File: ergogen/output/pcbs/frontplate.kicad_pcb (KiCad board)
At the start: 2 copper layers, 134 x 92.7 mm, 0 parts

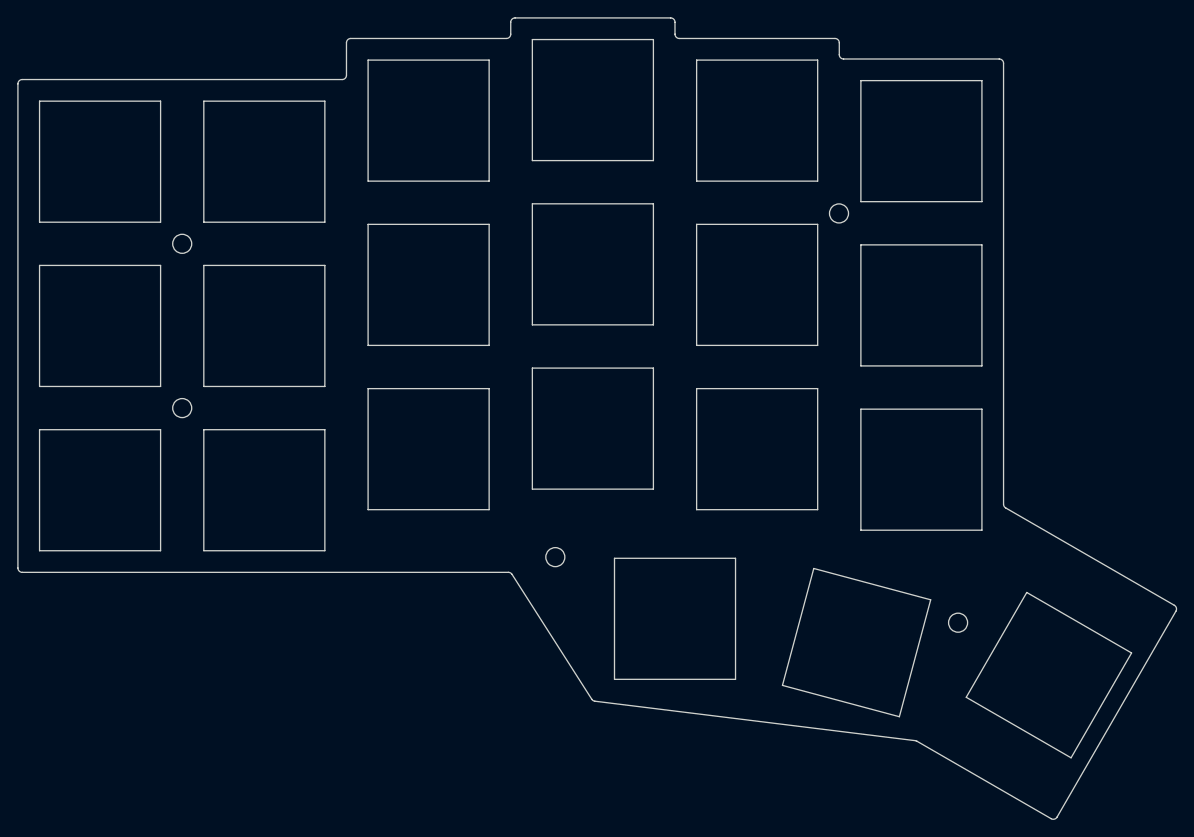
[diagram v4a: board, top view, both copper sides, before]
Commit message: Overhaul outlines making use of intersect
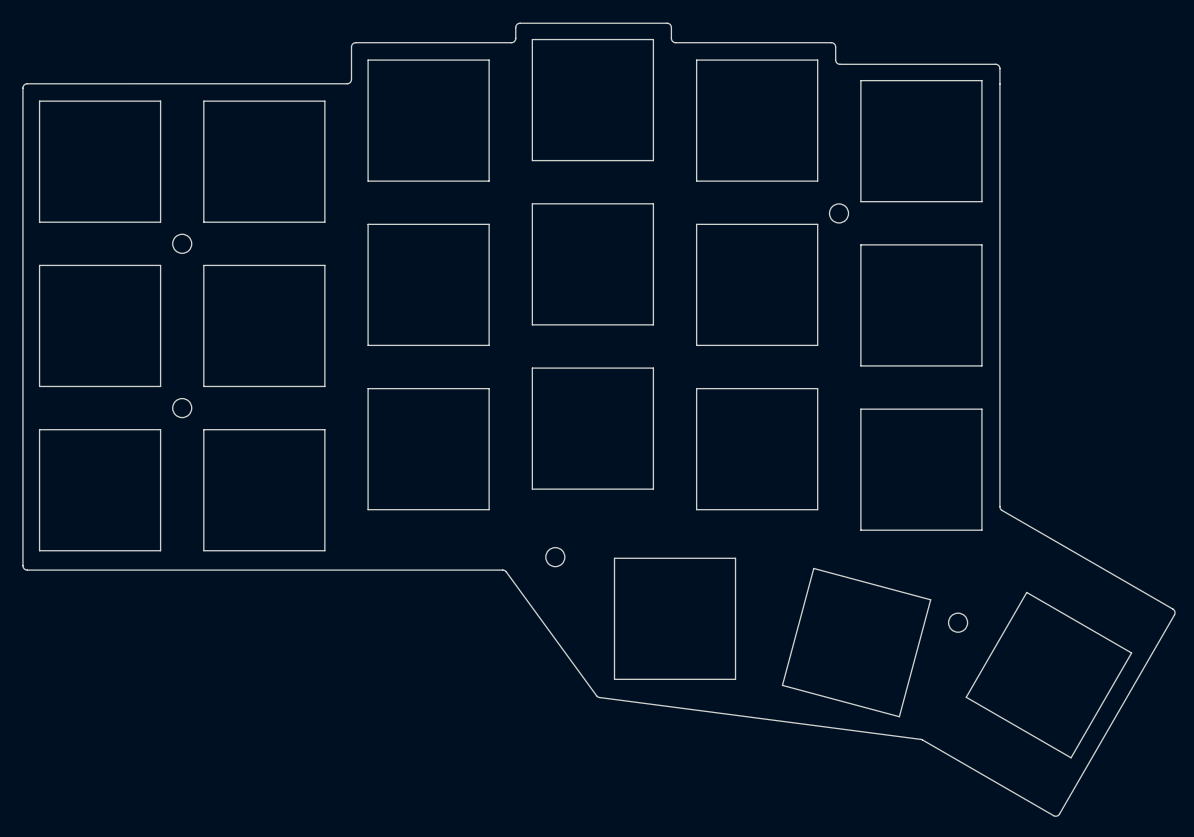
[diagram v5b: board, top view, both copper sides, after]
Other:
- board size 134 x 92.7 mm -> 133.3 x 91.7 mm
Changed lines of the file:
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@@
     (add_net "")
   )
-            (gr_line (start 91 109.5) (end 147.226056907563 109.5) (angle 90) (layer Edge.Cuts) (width 0.15))
-(gr_line (start 90.5 109) (end 90.5 53) (angle 90) (layer Edge.Cuts) (width 0.15))
-(gr_line (start 91 52.5) (end 128 52.5) (angle 90) (layer Edge.Cuts) (width 0.15))
-(gr_line (start 147 47.75) (end 129 47.75) (angle 90) (layer Edge.Cuts) (width 0.15))
-(gr_line (start 128.5 48.25) (end 128.5 52) (angle 90) (layer Edge.Cuts) (width 0.15))
-(gr_line (start 166.5 47.25) (end 166.5 45.875) (angle 90) (layer Edge.Cuts) (width 0.15))
-(gr_line (start 166 45.375) (end 148 45.375) (angle 90) (layer Edge.Cuts) (width 0.15))
-(gr_line (start 147.5 45.875) (end 147.5 47.25) (angle 90) (layer Edge.Cuts) (width 0.15))
-(gr_line (start 185.5 49.625) (end 185.5 48.25) (angle 90) (layer Edge.Cuts) (width 0.15))
-(gr_line (start 185 47.75) (end 167 47.75) (angle 90) (layer Edge.Cuts) (width 0.15))
-(gr_line (start 204.5 101.61675503683294) (end 204.5 50.625) (angle 90) (layer Edge.Cuts) (width 0.15))
-(gr_line (start 204 50.125) (end 186 50.125) (angle 90) (layer Edge.Cuts) (width 0.15))
-(gr_line (start 210.68768509880175 137.80950690032108) (end 224.43768510032112 113.99380830119821) (angle 90) (layer Edge.Cuts) (width 0.15))
-(gr_line (start 204.75000000000003 102.04976773683296) (end 224.25467240032103 113.31079560119827) (angle 90) (layer Edge.Cuts) (width 0.15))
-(gr_line (start 194.4825814717975 129.0308362223767) (end 210.00467239880174 137.99251960032112) (angle 90) (layer Edge.Cuts) (width 0.15))
-(gr_line (start 147.6474496930774 109.73087517731855) (end 156.87331650010177 124.17664030936987) (angle 90) (layer Edge.Cuts) (width 0.15))
-(gr_line (start 157.23359753636308 124.40376678062299) (end 194.2936932210506 128.9675976284421) (angle 90) (layer Edge.Cuts) (width 0.15))
-(gr_arc (start 147.226056907563 110) (end 147.647449607563 109.7308752) (angle -57.4354397170889) (layer Edge.Cuts) (width 0.15))
-(gr_arc (start 157.2947092856161 123.90751548668835) (end 156.8733165856161 124.17664028668835) (angle -50.414995185869486) (layer Edge.Cuts) (width 0.15))
-(gr_arc (start 194.23258147179752 129.4638489223767) (end 194.48258147179752 129.0308362223767) (angle -22.979555577197353) (layer Edge.Cuts) (width 0.15))
-(gr_arc (start 210.25467239880174 137.5595069003211) (end 210.00467239880174 137.99251960032112) (angle -90.00000000000279) (layer Edge.Cuts) (width 0.15))
-(gr_arc (start 224.00467240032108 113.74380830119827) (end 224.4376851003211 113.99380830119827) (angle -89.99999999999831) (layer Edge.Cuts) (width 0.15))
-(gr_arc (start 205 101.61675503683294) (end 204.5 101.61675503683294) (angle -59.999999891587805) (layer Edge.Cuts) (width 0.15))
-(gr_arc (start 204 50.625) (end 204.5 50.625) (angle -90) (layer Edge.Cuts) (width 0.15))
-(gr_arc (start 186 49.625) (end 185.5 49.625) (angle -90) (layer Edge.Cuts) (width 0.15))
-(gr_arc (start 185 48.25) (end 185.5 48.25) (angle -90) (layer Edge.Cuts) (width 0.15))
-(gr_arc (start 167 47.25) (end 166.5 47.25) (angle -90) (layer Edge.Cuts) (width 0.15))
-(gr_arc (start 166 45.875) (end 166.5 45.875) (angle -90) (layer Edge.Cuts) (width 0.15))
-(gr_arc (start 148 45.875) (end 148 45.375) (angle -90) (layer Edge.Cuts) (width 0.15))
-(gr_arc (start 147 47.25) (end 147 47.75) (angle -90) (layer Edge.Cuts) (width 0.15))
-(gr_arc (start 129 48.25) (end 129 47.75) (angle -90) (layer Edge.Cuts) (width 0.15))
-(gr_arc (start 128 52) (end 128 52.5) (angle -90) (layer Edge.Cuts) (width 0.15))
-(gr_arc (start 91 53) (end 91 52.5) (angle -90) (layer Edge.Cuts) (width 0.15))
-(gr_arc (start 91 109) (end 90.5 109) (angle -90) (layer Edge.Cuts) (width 0.15))
+            (gr_line (start 91.08198222285509 108.74001780012622) (end 91.08001777794281 53.49000464193523) (angle 90) (layer Edge.Cuts) (width 0.15))
+(gr_line (start 91.58000462794281 52.98998684198348) (end 128.58001314999998 52.98901315754868) (angle 90) (layer Edge.Cuts) (width 0.15))
+(gr_line (start 129.08 52.48901315754736) (end 129.08 48.74) (angle 90) (layer Edge.Cuts) (width 0.15))
+(gr_line (start 129.58 48.24) (end 147.58 48.24) (angle 90) (layer Edge.Cuts) (width 0.15))
+(gr_line (start 148.08 47.74) (end 148.08 46.488) (angle 90) (layer Edge.Cuts) (width 0.15))
+(gr_line (start 148.58 45.988) (end 165.582 45.988) (angle 90) (layer Edge.Cuts) (width 0.15))
+(gr_line (start 166.082 46.488) (end 166.082 47.74) (angle 90) (layer Edge.Cuts) (width 0.15))
+(gr_line (start 166.582 48.24) (end 184.581 48.24) (angle 90) (layer Edge.Cuts) (width 0.15))
+(gr_line (start 185.081 48.74) (end 185.081 50.238) (angle 90) (layer Edge.Cuts) (width 0.15))
+(gr_line (start 185.581 50.738) (end 203.58222192628773 50.738) (angle 90) (layer Edge.Cuts) (width 0.15))
+(gr_line (start 204.08222192628773 51.23777800000971) (end 204.083 52.98999999999069) (angle 90) (layer Edge.Cuts) (width 0.15))
+(gr_line (start 204.083 52.99022199999308) (end 204.083 101.90976811661676) (angle 90) (layer Edge.Cuts) (width 0.15))
+(gr_line (start 204.333 102.34278081661677) (end 224.08500381954127 113.74660553865856) (angle 90) (layer Edge.Cuts) (width 0.15))
+(gr_line (start 224.26802603203956 114.42960171700884) (end 210.97353193043915 137.45836746290382) (angle 90) (layer Edge.Cuts) (width 0.15))
+(gr_line (start 210.29050971794075 137.64139668455357) (end 195.12364206223265 128.884801539137) (angle 90) (layer Edge.Cuts) (width 0.15))
+(gr_line (start 194.9382670622326 128.82200823913698) (end 157.77283771855778 123.97774197949536) (angle 90) (layer Edge.Cuts) (width 0.15))
+(gr_line (start 157.43351074236324 123.77659301213079) (end 146.97978450304703 109.44534296736454) (angle 90) (layer Edge.Cuts) (width 0.15))
+(gr_line (start 146.57583252685248 109.24) (end 91.58198222285512 109.24) (angle 90) (layer Edge.Cuts) (width 0.15))
+(gr_arc (start 91.58001777794281 53.48998684156686) (end 91.58000457794282 52.98998684156686) (angle -90.00053289295953) (layer Edge.Cuts) (width 0.15))
+(gr_arc (start 128.58 52.48901315754736) (end 128.5800131 52.98901315754736) (angle -89.99849312100235) (layer Edge.Cuts) (width 0.15))
+(gr_arc (start 129.58 48.74) (end 129.58 48.24) (angle -90) (layer Edge.Cuts) (width 0.15))
+(gr_arc (start 147.58 47.74) (end 147.58 48.24) (angle -90) (layer Edge.Cuts) (width 0.15))
+(gr_arc (start 148.58 46.488) (end 148.58 45.988) (angle -90) (layer Edge.Cuts) (width 0.15))
+(gr_arc (start 165.582 46.488) (end 166.082 46.488) (angle -90) (layer Edge.Cuts) (width 0.15))
+(gr_arc (start 166.582 47.74) (end 166.082 47.74) (angle -90) (layer Edge.Cuts) (width 0.15))
+(gr_arc (start 184.581 48.74) (end 185.081 48.74) (angle -90) (layer Edge.Cuts) (width 0.15))
+(gr_arc (start 185.581 50.238) (end 185.081 50.238) (angle -90) (layer Edge.Cuts) (width 0.15))
+(gr_arc (start 203.58222192628773 51.238) (end 204.08222192628773 51.237778) (angle -89.97456067668081) (layer Edge.Cuts) (width 0.15))
+(gr_arc (start 203.583 52.99022199999308) (end 204.083 52.99022199999308) (angle -0.025439324706622683) (layer Edge.Cuts) (width 0.15))
+(gr_arc (start 204.583 101.90976811661676) (end 204.083 101.90976811661676) (angle -59.999999891584196) (layer Edge.Cuts) (width 0.15))
+(gr_arc (start 223.83500381954124 114.17961823865855) (end 224.26802601954125 114.42960173865855) (angle -89.99781537856549) (layer Edge.Cuts) (width 0.15))
+(gr_arc (start 210.54050971794078 137.20838398455356) (end 210.29050971794078 137.64139668455357) (angle -90.0021846214398) (layer Edge.Cuts) (width 0.15))
+(gr_arc (start 194.87364206223262 129.31781423913696) (end 195.12364206223262 128.88480153913696) (angle -22.57374496727097) (layer Edge.Cuts) (width 0.15))
+(gr_arc (start 157.83746271855782 123.48193597949538) (end 157.4335107185578 123.77659307949537) (angle -46.46539472382716) (layer Edge.Cuts) (width 0.15))
+(gr_arc (start 146.57583252685248 109.74) (end 146.97978452685248 109.4453429) (angle -53.89164986497705) (layer Edge.Cuts) (width 0.15))
+(gr_arc (start 91.58198222285512 108.74) (end 91.08198222285512 108.74001779999999) (angle -89.99796025578533) (layer Edge.Cuts) (width 0.15))
 (gr_line (start 93 107) (end 107 107) (angle 90) (layer Edge.Cuts) (width 0.15))
 (gr_line (start 107 107) (end 107 93) (angle 90) (layer Edge.Cuts) (width 0.15))

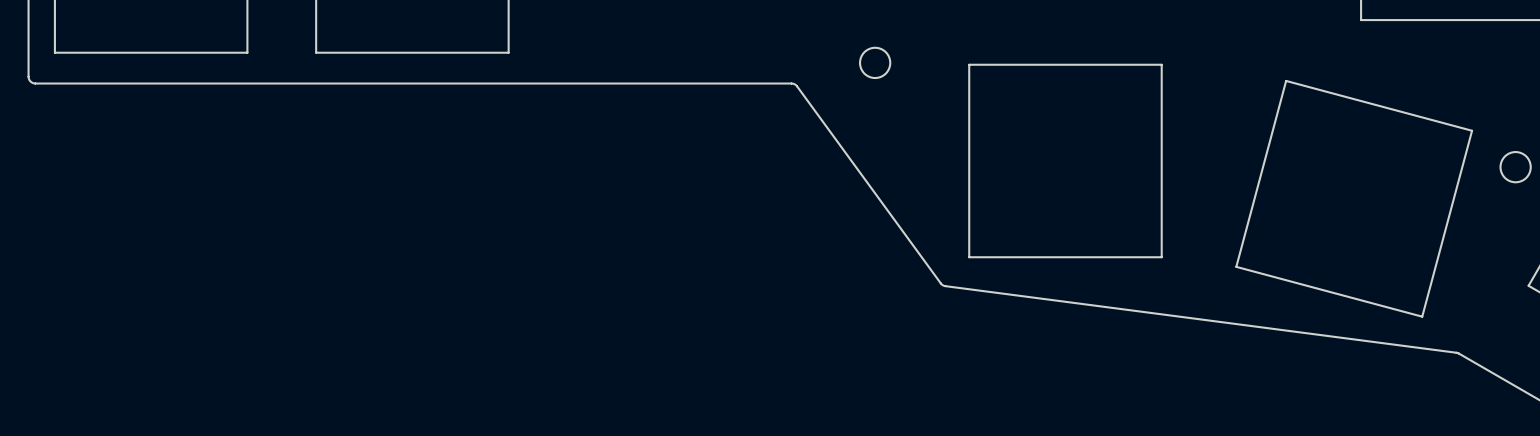
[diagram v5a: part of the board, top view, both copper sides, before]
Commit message: Change to relative measures for helper points
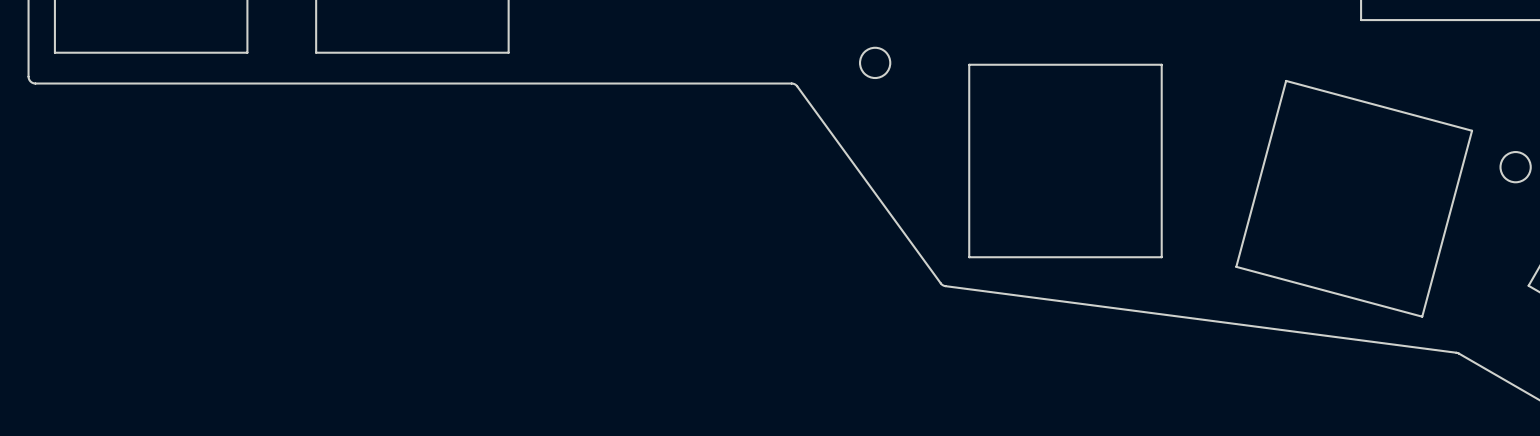
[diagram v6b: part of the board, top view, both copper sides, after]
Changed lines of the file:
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@@
 (gr_line (start 224.26802603203956 114.42960171700884) (end 210.97353193043915 137.45836746290382) (angle 90) (layer Edge.Cuts) (width 0.15))
 (gr_line (start 210.29050971794075 137.64139668455357) (end 195.12364206223265 128.884801539137) (angle 90) (layer Edge.Cuts) (width 0.15))
-(gr_line (start 194.9382670622326 128.82200823913698) (end 157.77283771855778 123.97774197949536) (angle 90) (layer Edge.Cuts) (width 0.15))
-(gr_line (start 157.43351074236324 123.77659301213079) (end 146.97978450304703 109.44534296736454) (angle 90) (layer Edge.Cuts) (width 0.15))
-(gr_line (start 146.57583252685248 109.24) (end 91.58198222285512 109.24) (angle 90) (layer Edge.Cuts) (width 0.15))
+(gr_line (start 194.9382670622326 128.82200823913698) (end 157.77296812333506 123.97775897688982) (angle 90) (layer Edge.Cuts) (width 0.15))
+(gr_line (start 157.43351034067848 123.77643070068846) (end 146.98977558129695 109.44552227620129) (angle 90) (layer Edge.Cuts) (width 0.15))
+(gr_line (start 146.5856927986404 109.24) (end 91.58198222285512 109.24) (angle 90) (layer Edge.Cuts) (width 0.15))
 (gr_arc (start 91.58001777794281 53.48998684156686) (end 91.58000457794282 52.98998684156686) (angle -90.00053289295953) (layer Edge.Cuts) (width 0.15))
 (gr_arc (start 128.58 52.48901315754736) (end 128.5800131 52.98901315754736) (angle -89.99849312100235) (layer Edge.Cuts) (width 0.15))
@@
 (gr_arc (start 210.54050971794078 137.20838398455356) (end 210.29050971794078 137.64139668455357) (angle -90.0021846214398) (layer Edge.Cuts) (width 0.15))
 (gr_arc (start 194.87364206223262 129.31781423913696) (end 195.12364206223262 128.88480153913696) (angle -22.57374496727097) (layer Edge.Cuts) (width 0.15))
-(gr_arc (start 157.83746271855782 123.48193597949538) (end 157.4335107185578 123.77659307949537) (angle -46.46539472382716) (layer Edge.Cuts) (width 0.15))
-(gr_arc (start 146.57583252685248 109.74) (end 146.97978452685248 109.4453429) (angle -53.89164986497705) (layer Edge.Cuts) (width 0.15))
+(gr_arc (start 157.83759312333507 123.48195297688983) (end 157.43351032333507 123.77643067688983) (angle -46.490828368152734) (layer Edge.Cuts) (width 0.15))
+(gr_arc (start 146.5856927986404 109.73999999999998) (end 146.9897755986404 109.44552229999998) (angle -53.917083509298145) (layer Edge.Cuts) (width 0.15))
 (gr_arc (start 91.58198222285512 108.74) (end 91.08198222285512 108.74001779999999) (angle -89.99796025578533) (layer Edge.Cuts) (width 0.15))
 (gr_line (start 93 107) (end 107 107) (angle 90) (layer Edge.Cuts) (width 0.15))

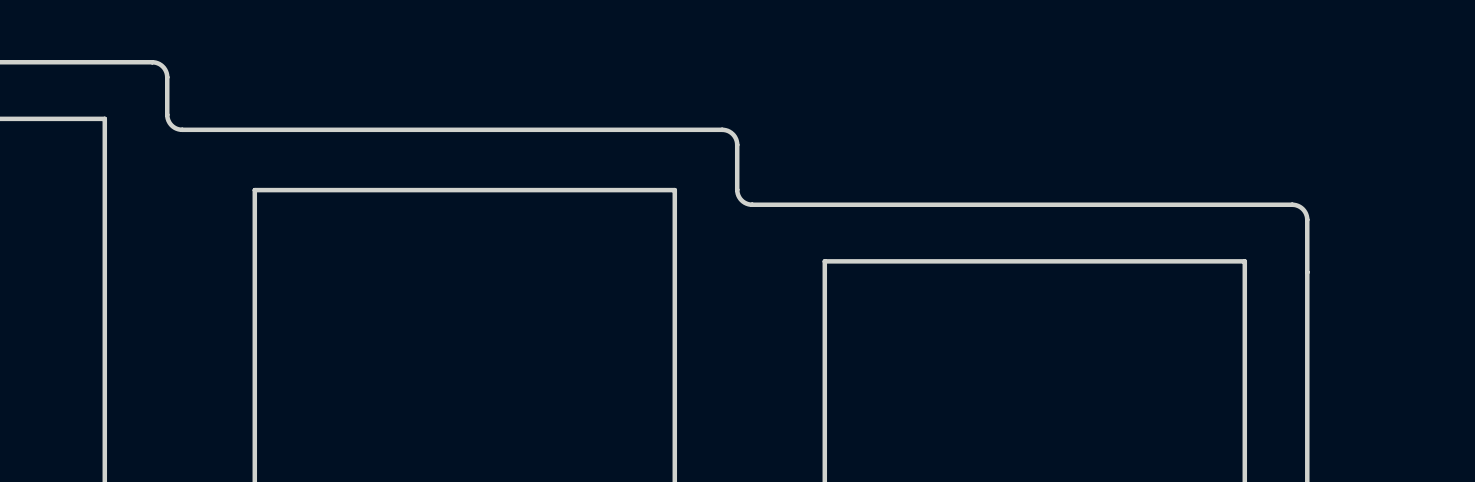
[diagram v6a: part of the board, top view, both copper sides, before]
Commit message: Add missing parametric measures
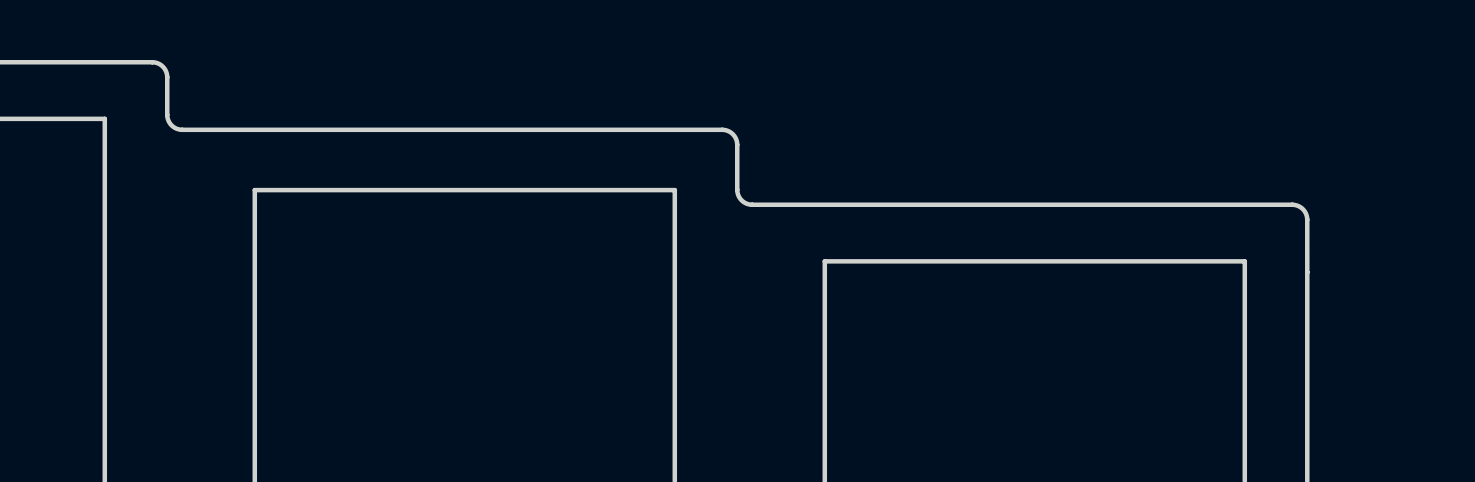
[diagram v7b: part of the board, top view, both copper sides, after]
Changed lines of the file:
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@@
 (gr_line (start 148.58 45.988) (end 165.582 45.988) (angle 90) (layer Edge.Cuts) (width 0.15))
 (gr_line (start 166.082 46.488) (end 166.082 47.74) (angle 90) (layer Edge.Cuts) (width 0.15))
-(gr_line (start 166.582 48.24) (end 184.581 48.24) (angle 90) (layer Edge.Cuts) (width 0.15))
-(gr_line (start 185.081 48.74) (end 185.081 50.238) (angle 90) (layer Edge.Cuts) (width 0.15))
-(gr_line (start 185.581 50.738) (end 203.58222192628773 50.738) (angle 90) (layer Edge.Cuts) (width 0.15))
+(gr_line (start 166.582 48.24) (end 184.582 48.24) (angle 90) (layer Edge.Cuts) (width 0.15))
+(gr_line (start 185.082 48.74) (end 185.082 50.238) (angle 90) (layer Edge.Cuts) (width 0.15))
+(gr_line (start 185.582 50.738) (end 203.58222192628773 50.738) (angle 90) (layer Edge.Cuts) (width 0.15))
 (gr_line (start 204.08222192628773 51.23777800000971) (end 204.083 52.98999999999069) (angle 90) (layer Edge.Cuts) (width 0.15))
 (gr_line (start 204.083 52.99022199999308) (end 204.083 101.90976811661676) (angle 90) (layer Edge.Cuts) (width 0.15))
@@
 (gr_arc (start 165.582 46.488) (end 166.082 46.488) (angle -90) (layer Edge.Cuts) (width 0.15))
 (gr_arc (start 166.582 47.74) (end 166.082 47.74) (angle -90) (layer Edge.Cuts) (width 0.15))
-(gr_arc (start 184.581 48.74) (end 185.081 48.74) (angle -90) (layer Edge.Cuts) (width 0.15))
-(gr_arc (start 185.581 50.238) (end 185.081 50.238) (angle -90) (layer Edge.Cuts) (width 0.15))
+(gr_arc (start 184.582 48.74) (end 185.082 48.74) (angle -90) (layer Edge.Cuts) (width 0.15))
+(gr_arc (start 185.582 50.238) (end 185.082 50.238) (angle -90) (layer Edge.Cuts) (width 0.15))
 (gr_arc (start 203.58222192628773 51.238) (end 204.08222192628773 51.237778) (angle -89.97456067668081) (layer Edge.Cuts) (width 0.15))
 (gr_arc (start 203.583 52.99022199999308) (end 204.083 52.99022199999308) (angle -0.025439324706622683) (layer Edge.Cuts) (width 0.15))
